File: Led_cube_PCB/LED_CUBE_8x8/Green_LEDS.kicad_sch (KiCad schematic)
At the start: 34 parts, among them IC1 74AHCT244PW,118, IC10 74AHCT244PW,118, IC11 74AHCT244PW,118, IC12 74AHCT244PW,118, IC2 74AHCT244PW,118, IC26 74AHC138PW,118, IC3 74AHCT244PW,118, IC8 74AHCT244PW,118, IC9 74AHCT244PW,118

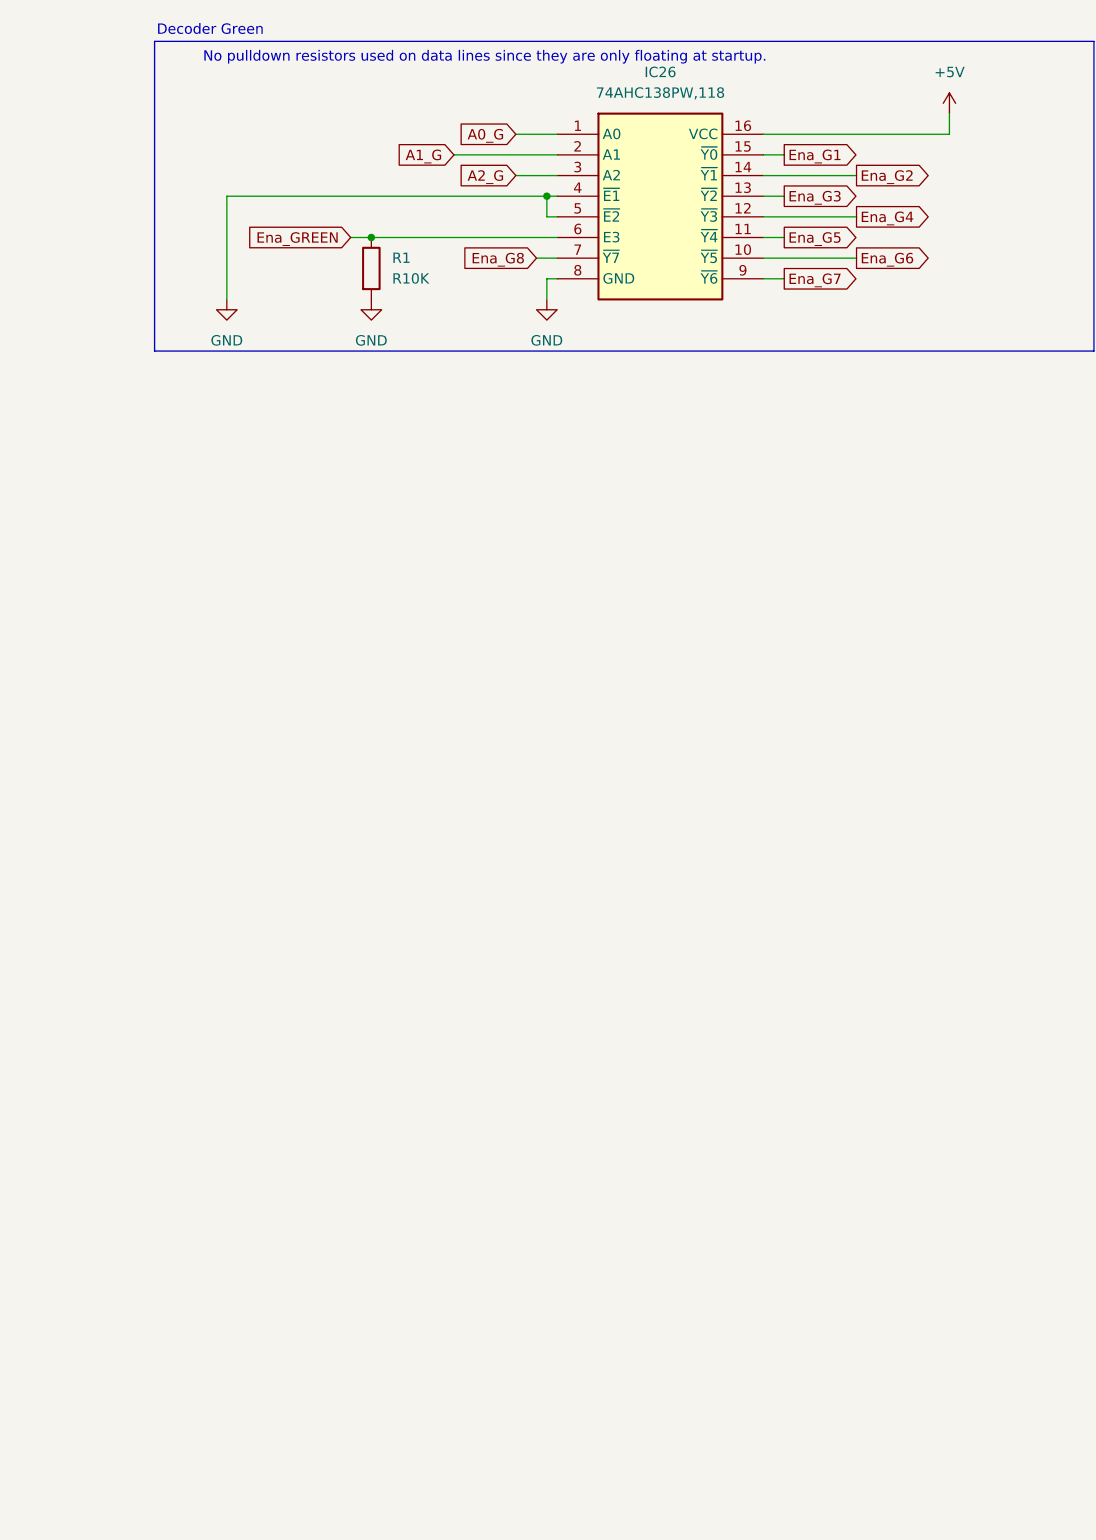
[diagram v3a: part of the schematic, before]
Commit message: added spice simulations folder, For simulating transients effect on the power buck converter. Also finished layer select in eeschema.
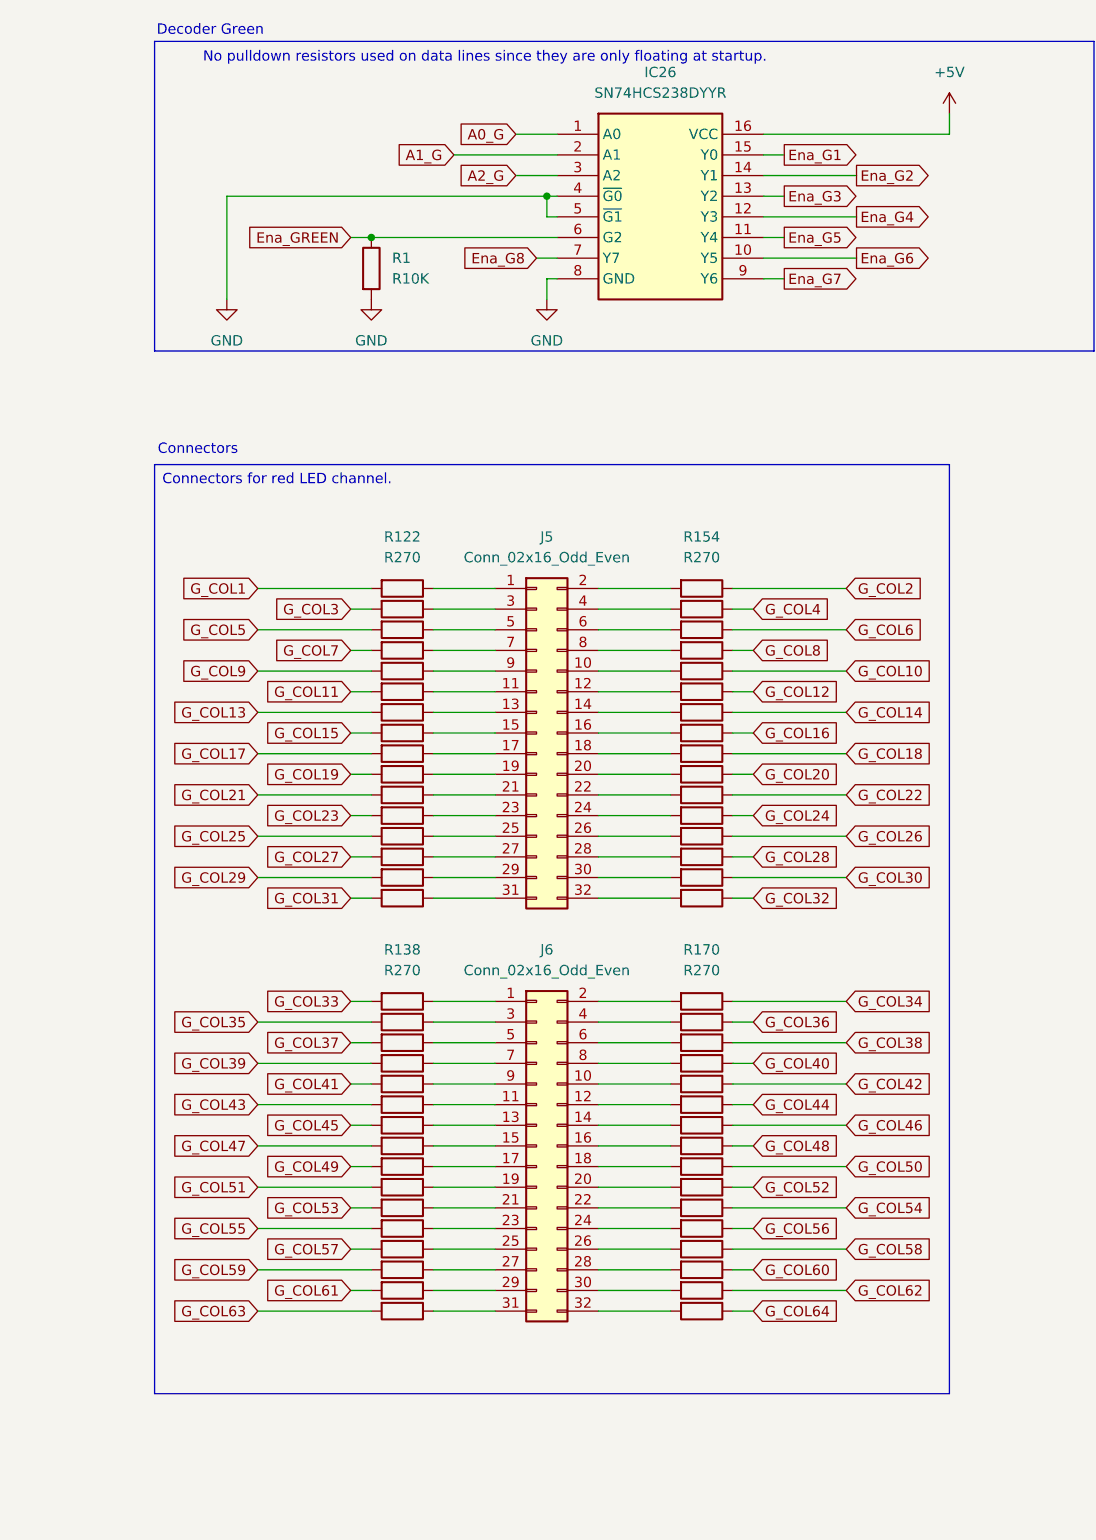
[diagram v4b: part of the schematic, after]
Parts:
- removed IC26: 74AHC138PW,118, SOP65P640X110-16N, symbol SamacSys_Parts:74AHC138PW,118
- added IC26: SN74HCS238DYYR, SOP50P326X110-16N, symbol SamacSys_Parts:SN74HCS238DYYR
- added J5, J6: Conn_02x16_Odd_Even, Connector_PinHeader_1.00mm:PinHeader_2x16_P1.00mm_Vertical, symbol Connector_Generic:Conn_02x16_Odd_Even
- added R122, R123, R124, R125, R126, R127, R128, R129, R130, R131, R132, R133, R134, R135, R136, R137, R138, R139, R140, R141, R142, R143, R144, R145, R146, R147, R148, R149, R150, R151, R152, R153, R154, R155, R156, R157, R158, R159, R160, R161, R162, R163, R164, R165, R166, R167, R168, R169, R170, R171, R172, R173, R174, R175, R176, R177, R178, R179, R180, R181, R182, R183, R184, R185: R270, symbol Device:R
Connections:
- net +5V: now also IC26.16 (VCC)
- net A0_G: now also IC26.1 (A0)
- net A1_G: now also IC26.2 (A1)
- net A2_G: now also IC26.3 (A2)
- net Ena_G1: now also IC26.15 (Y0)
- net Ena_G2: now also IC26.14 (Y1)
- net Ena_G3: now also IC26.13 (Y2)
- net Ena_G4: now also IC26.12 (Y3)
- net Ena_G5: now also IC26.11 (Y4)
- net Ena_G6: now also IC26.10 (Y5)
- net Ena_G7: now also IC26.9 (Y6)
- net Ena_G8: now also IC26.7 (Y7)
- net Ena_GREEN: now also IC26.6 (G2)
- net GND: now also IC26.4 (~{G0}), IC26.5 (~{G1}), IC26.8 (GND)
- net G_COL1: now also R122.2
- net G_COL10: now also R158.1
- net G_COL11: now also R127.2
- net G_COL12: now also R159.1
- net G_COL13: now also R128.2
- net G_COL14: now also R160.1
- net G_COL15: now also R129.2
- net G_COL16: now also R161.1
- net G_COL17: now also R130.2
- net G_COL18: now also R162.1
- net G_COL19: now also R131.2
- net G_COL2: now also R154.1
- net G_COL20: now also R163.1
- net G_COL21: now also R132.2
- net G_COL22: now also R164.1
- net G_COL23: now also R133.2
- net G_COL24: now also R165.1
- net G_COL25: now also R134.2
- net G_COL26: now also R166.1
- net G_COL27: now also R135.2
- net G_COL28: now also R167.1
- net G_COL29: now also R136.2
- net G_COL3: now also R123.2
- net G_COL30: now also R168.1
- net G_COL31: now also R137.2
- net G_COL32: now also R169.1
- net G_COL33: now also R138.2
- net G_COL34: now also R170.1
- net G_COL35: now also R139.2
- net G_COL36: now also R171.1
- net G_COL37: now also R140.2
- net G_COL38: now also R172.1
- net G_COL39: now also R141.2
- net G_COL4: now also R155.1
- net G_COL40: now also R173.1
- net G_COL41: now also R142.2
- net G_COL42: now also R174.1
- net G_COL43: now also R143.2
- net G_COL44: now also R175.1
- net G_COL45: now also R144.2
- net G_COL46: now also R176.1
- net G_COL47: now also R145.2
- net G_COL48: now also R177.1
- net G_COL49: now also R146.2
- net G_COL5: now also R124.2
- net G_COL50: now also R178.1
- net G_COL51: now also R147.2
- net G_COL52: now also R179.1
- net G_COL53: now also R148.2
- net G_COL54: now also R180.1
- net G_COL55: now also R149.2
- net G_COL56: now also R181.1
- net G_COL57: now also R150.2
- net G_COL58: now also R182.1
- net G_COL59: now also R151.2
- net G_COL6: now also R156.1
- net G_COL60: now also R183.1
- net G_COL61: now also R152.2
- net G_COL62: now also R184.1
- net G_COL63: now also R153.2
- net G_COL64: now also R185.1
- net G_COL7: now also R125.2
- net G_COL8: now also R157.1
- net G_COL9: now also R126.2
- new net: J5.11 (Pin_11), R127.1
- new net: J6.12 (Pin_12), R175.2
- new net: J5.9 (Pin_9), R126.1
- new net: J6.1 (Pin_1), R138.1
- new net: J5.26 (Pin_26), R166.2
- new net: J5.32 (Pin_32), R169.2
- new net: J6.18 (Pin_18), R178.2
- new net: J6.6 (Pin_6), R172.2
- new net: J5.6 (Pin_6), R156.2
- new net: J6.25 (Pin_25), R150.1
- new net: J6.21 (Pin_21), R148.1
- new net: J6.7 (Pin_7), R141.1
- new net: J5.20 (Pin_20), R163.2
- new net: J5.5 (Pin_5), R124.1
- new net: J6.31 (Pin_31), R153.1
- new net: J5.2 (Pin_2), R154.2
- new net: J6.5 (Pin_5), R140.1
- new net: J6.4 (Pin_4), R171.2
- new net: J6.10 (Pin_10), R174.2
- new net: J6.11 (Pin_11), R143.1
- new net: J6.13 (Pin_13), R144.1
- new net: J6.14 (Pin_14), R176.2
- new net: J6.15 (Pin_15), R145.1
- new net: J6.16 (Pin_16), R177.2
- new net: J6.17 (Pin_17), R146.1
- new net: J6.19 (Pin_19), R147.1
- new net: J6.2 (Pin_2), R170.2
- new net: J6.20 (Pin_20), R179.2
- new net: J6.22 (Pin_22), R180.2
- new net: J6.23 (Pin_23), R149.1
- new net: J6.24 (Pin_24), R181.2
- new net: J6.26 (Pin_26), R182.2
- new net: J6.27 (Pin_27), R151.1
- new net: J6.28 (Pin_28), R183.2
- new net: J6.29 (Pin_29), R152.1
- new net: J6.3 (Pin_3), R139.1
- new net: J6.30 (Pin_30), R184.2
- new net: J6.32 (Pin_32), R185.2
- new net: J6.8 (Pin_8), R173.2
- new net: J6.9 (Pin_9), R142.1
- new net: J5.8 (Pin_8), R157.2
- new net: J5.18 (Pin_18), R162.2
- new net: J5.1 (Pin_1), R122.1
- new net: J5.10 (Pin_10), R158.2
- new net: J5.12 (Pin_12), R159.2
- new net: J5.13 (Pin_13), R128.1
- new net: J5.14 (Pin_14), R160.2
- new net: J5.15 (Pin_15), R129.1
- new net: J5.16 (Pin_16), R161.2
- new net: J5.17 (Pin_17), R130.1
- new net: J5.19 (Pin_19), R131.1
- new net: J5.21 (Pin_21), R132.1
- new net: J5.22 (Pin_22), R164.2
- new net: J5.23 (Pin_23), R133.1
- new net: J5.24 (Pin_24), R165.2
- new net: J5.25 (Pin_25), R134.1
- new net: J5.27 (Pin_27), R135.1
- new net: J5.28 (Pin_28), R167.2
- new net: J5.29 (Pin_29), R136.1
- new net: J5.3 (Pin_3), R123.1
- new net: J5.30 (Pin_30), R168.2
- new net: J5.31 (Pin_31), R137.1
- new net: J5.4 (Pin_4), R155.2
- new net: J5.7 (Pin_7), R125.1
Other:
- note added: "Connectors"
